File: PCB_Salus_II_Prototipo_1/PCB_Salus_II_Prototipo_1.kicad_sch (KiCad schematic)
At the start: 52 parts, among them J1 Servo1, J10 Conn_01x07_Pin, J11 Conector Entrada 5V, J12 Conector 5V, J13 Conector Entrada 7V, J14 Conector Salida 7V, J15 Sensor 1, J16 Luz2, J17 Cambios1, J18 Cambios 2, J19 MarchaAtras1, J2 Sensor Giro, J20 MarchaAtras2, J21 Sobrante1, J22 Sobrante2, J23 Arranque1, J24 Arranque2, J25 ControlMotor, J26 Sensor 2, J27 Sensor 3, J28 Sensor 4, J29 Sensor 5, J3 Acelerador, J30 Sensor 6, J31 Sensor 7, J4 Conn_01x05_Pin, J5 Servo2, J6 Antena, J7 SensorGiro, J8 Luz1, J9 Conn_01x07_Pin, K1 Rele 5V, K2 Rele 7V, K3 Arranque, Q1 IO25, Q2 IO26, Q3 IO27, Q4 IO14, U1 ESP32-DEVKITC-32D, U2 RASPBERRY_PI_4B_4GB

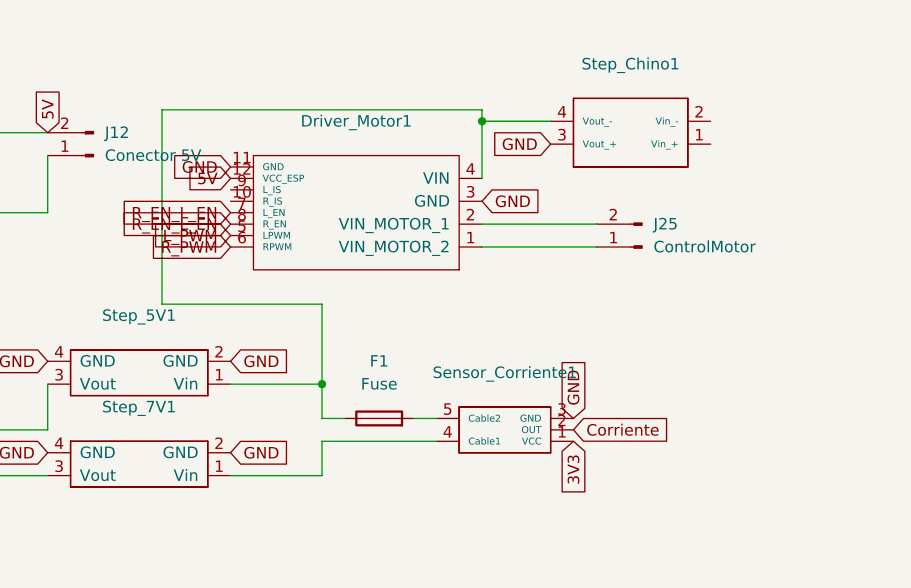
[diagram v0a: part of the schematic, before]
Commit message: Se cambio la Ip para configurarlacon WiFi
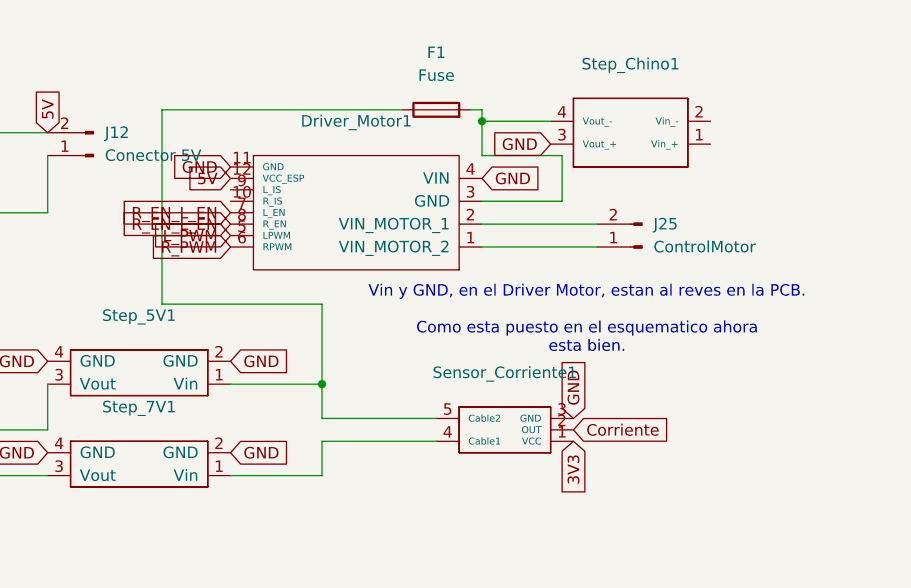
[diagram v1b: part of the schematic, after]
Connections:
- net GND: now also Driver_Motor1.4 (VIN); no longer Driver_Motor1.3 (GND)
- net at F1.1, Step_5V1.1 (Vin): now also Sensor_Corriente1.5 (Cable2); no longer Driver_Motor1.4 (VIN), Step_Chino1.4 (Vout_-)
- net at F1.2: now also Driver_Motor1.3 (GND), Step_Chino1.4 (Vout_-); no longer Sensor_Corriente1.5 (Cable2)
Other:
- note added: "Vin y GND, en el Driver Motor, estan al reves en la PCB. Como esta puesto en el esquematico ahora esta bien."
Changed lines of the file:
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@@
 	)
 	(junction
-		(at 259.08 19.05)
-		(diameter 0)
-		(color 0 0 0 0)
-	)
-	(junction
 		(at 209.55 101.6)
 		(diameter 0)
@@
 	)
 	(junction
+		(at 259.08 19.05)
+		(diameter 0)
+		(color 0 0 0 0)
+	)
+	(junction
 		(at 241.3 48.26)
 		(diameter 0)
@@
 	(wire
 		(pts
-			(xy 251.46 52.07) (xy 254 52.07)
+			(xy 264.16 96.52) (xy 271.78 96.52)
 		)
 		(stroke
@@
 	(wire
 		(pts
-			(xy 264.16 96.52) (xy 271.78 96.52)
+			(xy 267.97 27.94) (xy 267.97 22.86)
 		)
 		(stroke
@@
 	(wire
 		(pts
-			(xy 223.52 17.78) (xy 259.08 17.78)
+			(xy 223.52 17.78) (xy 250.19 17.78)
 		)
 		(stroke
@@
 	(wire
 		(pts
-			(xy 241.3 52.07) (xy 243.84 52.07)
+			(xy 241.3 52.07) (xy 254 52.07)
+		)
+		(stroke
+			(width 0)
+			(type default)
+		)
+	)
+	(wire
+		(pts
+			(xy 257.81 17.78) (xy 259.08 17.78)
 		)
 		(stroke
@@
 	(wire
 		(pts
-			(xy 53.34 167.64) (xy 53.34 176.53)
+			(xy 259.08 27.94) (xy 267.97 27.94)
 		)
 		(stroke
@@
 	(wire
 		(pts
-			(xy 224.79 101.6) (xy 224.79 95.25)
+			(xy 53.34 167.64) (xy 53.34 176.53)
 		)
 		(stroke
@@
 	(wire
 		(pts
-			(xy 88.9 54.61) (xy 67.31 54.61)
+			(xy 224.79 101.6) (xy 224.79 95.25)
 		)
 		(stroke
@@
 	(wire
 		(pts
-			(xy 259.08 19.05) (xy 259.08 25.4)
+			(xy 88.9 54.61) (xy 67.31 54.61)
 		)
 		(stroke
@@
 	(wire
 		(pts
+			(xy 259.08 19.05) (xy 259.08 22.86)
+		)
+		(stroke
+			(width 0)
+			(type default)
+		)
+	)
+	(wire
+		(pts
 			(xy 210.82 53.34) (xy 121.92 53.34)
 		)
@@
 	(wire
 		(pts
+			(xy 259.08 22.86) (xy 267.97 22.86)
+		)
+		(stroke
+			(width 0)
+			(type default)
+		)
+	)
+	(wire
+		(pts
 			(xy 120.65 170.18) (xy 120.65 179.07)
 		)
@@
 		)
 	)
+	(text "Vin y GND, en el Driver Motor, estan al reves en la PCB.\n\nComo esta puesto en el esquematico ahora \nesta bien."
+		(exclude_from_sim no)
+		(at 270.764 41.148 0)
+		(effects
+			(font
+				(size 1.27 1.27)
+			)
+		)
+	)
 	(text "SISTEMA SEGURIDAD 5V\n"
 		(exclude_from_sim no)
@@
 		)
 	)
-	(global_label "GND"
+	(global_label "5V"
 		(shape input)
-		(at 259.08 27.94 0)
+		(at 154.94 115.57 270)
 		(fields_autoplaced yes)
 		(effects
@@
 				(size 1.27 1.27)
 			)
-			(justify left)
+			(justify right)
 		)
 		(property "Intersheetrefs" "${INTERSHEET_REFS}"
-			(at 265.9357 27.94 0)
+			(at 154.94 120.8533 90)
 			(effects
 				(font
 					(size 1.27 1.27)
 				)
-				(justify left)
+				(justify right)
 				(hide yes)
 			)
 		)
 	)
-	(global_label "5V"
+	(global_label "Acelerador"
 		(shape input)
-		(at 154.94 115.57 270)
+		(at 67.31 49.53 0)
 		(fields_autoplaced yes)
 		(effects
@@
 				(size 1.27 1.27)
 			)
-			(justify right)
+			(justify left)
 		)
 		(property "Intersheetrefs" "${INTERSHEET_REFS}"
-			(at 154.94 120.8533 90)
+			(at 80.3342 49.53 0)
 			(effects
 				(font
 					(size 1.27 1.27)
 				)
-				(justify right)
+				(justify left)
 				(hide yes)
 			)
 		)
 	)
-	(global_label "Acelerador"
+	(global_label "Rele1"
 		(shape input)
-		(at 67.31 49.53 0)
+		(at 22.86 121.92 180)
 		(fields_autoplaced yes)
 		(effects
@@
 				(size 1.27 1.27)
 			)
-			(justify left)
+			(justify right)
 		)
 		(property "Intersheetrefs" "${INTERSHEET_REFS}"
-			(at 80.3342 49.53 0)
+			(at 14.5529 121.92 0)
 			(effects
 				(font
 					(size 1.27 1.27)
 				)
-				(justify left)
+				(justify right)
 				(hide yes)
 			)
 		)
 	)
-	(global_label "Rele1"
+	(global_label "GND"
 		(shape input)
-		(at 22.86 121.92 180)
+		(at 259.08 25.4 0)
 		(fields_autoplaced yes)
 		(effects
@@
 				(size 1.27 1.27)
 			)
-			(justify right)
+			(justify left)
 		)
 		(property "Intersheetrefs" "${INTERSHEET_REFS}"
-			(at 14.5529 121.92 0)
+			(at 265.9357 25.4 0)
 			(effects
 				(font
 					(size 1.27 1.27)
 				)
-				(justify right)
+				(justify left)
 				(hide yes)
 			)
@@
 	)
 	(symbol
-		(lib_id "Device:Fuse")
-		(at 247.65 52.07 90)
-		(unit 1)
-		(exclude_from_sim no)
-		(in_bom yes)
-		(on_board yes)
-		(dnp no)
-		(fields_autoplaced yes)
-		(property "Reference" "F1"
-			(at 247.65 45.72 90)
-			(effects
-				(font
-					(size 1.27 1.27)
-				)
-			)
-		)
-		(property "Value" "Fuse"
-			(at 247.65 48.26 90)
-			(effects
-				(font
-					(size 1.27 1.27)
-				)
-			)
-		)
-		(property "Footprint" "Fuse:Fuseholder_Clip-5x20mm_Eaton_1A5601-01_Inline_P20.80x6.76mm_D1.70mm_Horizontal"
-			(at 247.65 53.848 90)
-			(effects
-				(font
-					(size 1.27 1.27)
-				)
-				(hide yes)
-			)
-		)
-		(property "Datasheet" "~"
-			(at 247.65 52.07 0)
-			(effects
-				(font
-					(size 1.27 1.27)
-				)
-				(hide yes)
-			)
-		)
-		(property "Description" "Fuse"
-			(at 247.65 52.07 0)
-			(effects
-				(font
-					(size 1.27 1.27)
-				)
-				(hide yes)
-			)
-		)
-		(pin "2"
-		)
-		(pin "1"
-		)
-		(instances
-			(project ""
-				(path "/ba46b43d-a80c-4bb9-8819-4a9c21f18053"
-					(reference "F1")
-					(unit 1)
-				)
-			)
-		)
-	)
-	(symbol
 		(lib_id "Connector:Conn_01x02_Pin")
 		(at 135.89 124.46 0)
@@
 					(unit 1)
 				)
+			)
+		)
+	)
+	(symbol
+		(lib_id "Device:Fuse")
+		(at 254 17.78 90)
+		(unit 1)
+		(exclude_from_sim no)
+		(in_bom yes)
+		(on_board yes)
+		(dnp no)
+		(fields_autoplaced yes)
+		(property "Reference" "F1"
+			(at 254 11.43 90)
+			(effects
+				(font
+					(size 1.27 1.27)
+				)
+			)
+		)
+		(property "Value" "Fuse"
+			(at 254 13.97 90)
+			(effects
+				(font
+					(size 1.27 1.27)
+				)
+			)
+		)
+		(property "Footprint" "Fuse:Fuseholder_Clip-5x20mm_Eaton_1A5601-01_Inline_P20.80x6.76mm_D1.70mm_Horizontal"
+			(at 254 19.558 90)
+			(effects
+				(font
+					(size 1.27 1.27)
+				)
+				(hide yes)
+			)
+		)
+		(property "Datasheet" "~"
+			(at 254 17.78 0)
+			(effects
+				(font
+					(size 1.27 1.27)
+				)
+				(hide yes)
+			)
+		)
+		(property "Description" "Fuse"
+			(at 254 17.78 0)
+			(effects
+				(font
+					(size 1.27 1.27)
+				)
+				(hide yes)
+			)
+		)
+		(pin "2"
+		)
+		(pin "1"
+		)
+		(instances
+			(project "PCB_Salus_II_Prototipo_1"
+				(path "/ba46b43d-a80c-4bb9-8819-4a9c21f18053"
+					(reference "F1")
+					(unit 1)
+				)
